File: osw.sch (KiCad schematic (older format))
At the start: 59 parts, among them J1 Conn_01x02, J2 Conn_01x04, J3 Conn_01x02, Q1 2N7002, SW1 SW_Push, SW2 SW_Push, SW4 SW_Push, SW5 SW_Push, U1 DS3231MZ, U10 LTC3440EMS, U11 MCP73831T-2ACI_OT, U12 USBLC6-2SC6, U2 BMA400, U3 BMP280, U4 GC9A01_IPS_display, U5 USB-OTG, U6 CH340E, U7 ttgo-32-micro, U8 Quectel_L96, U9 TPS2115A

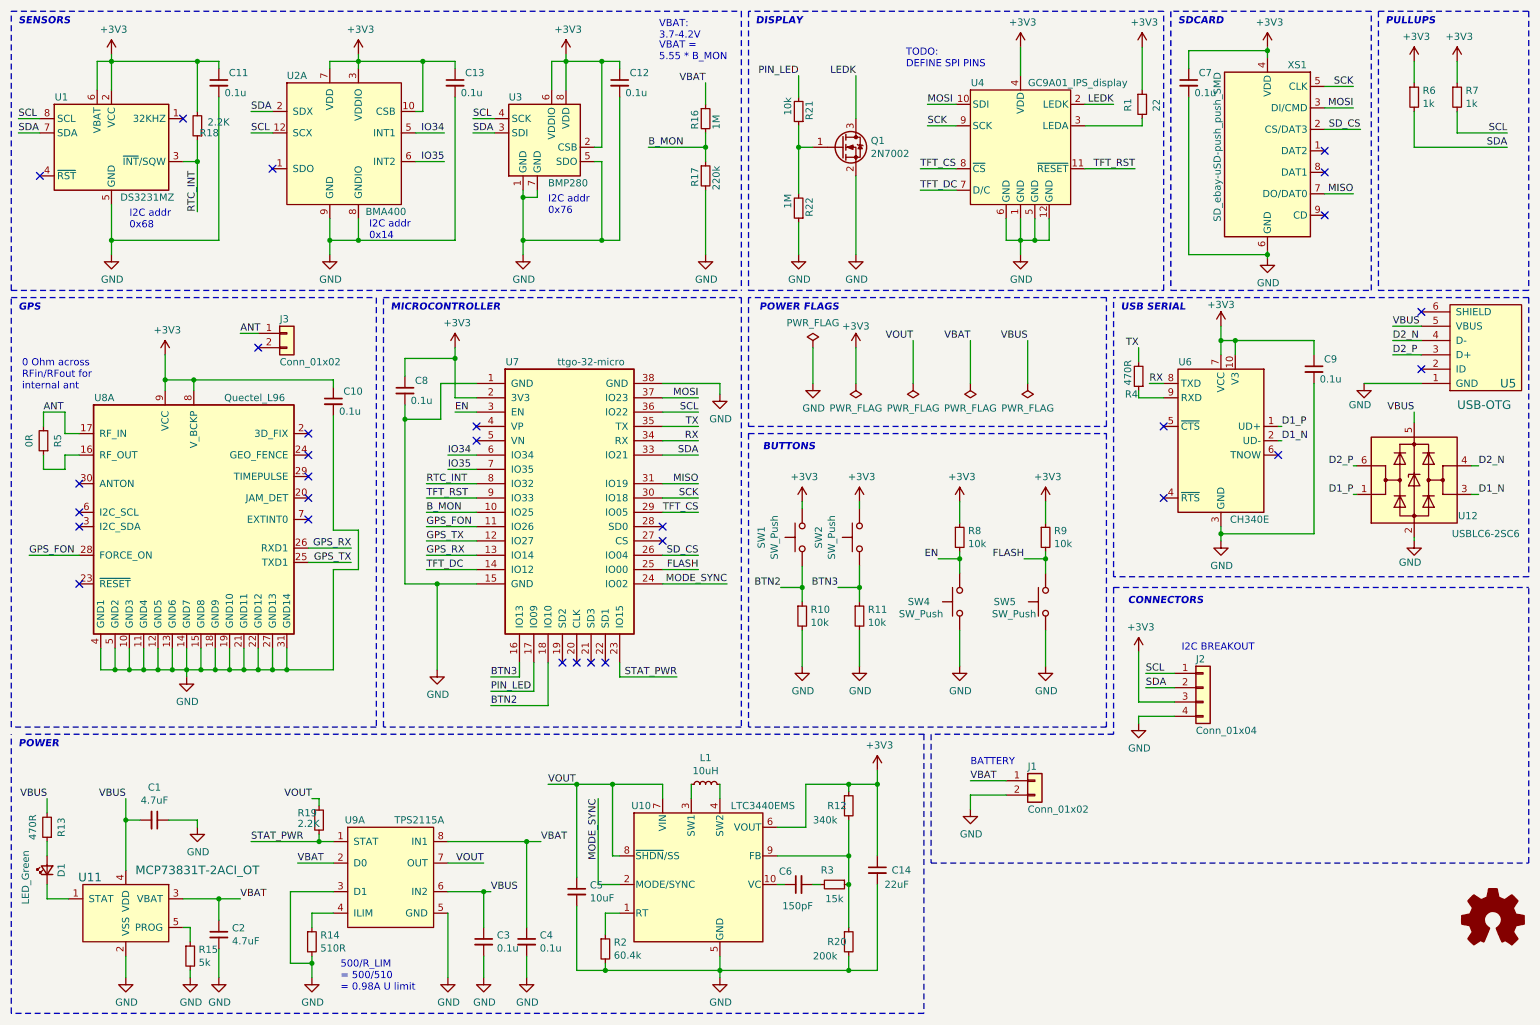
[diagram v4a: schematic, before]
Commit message: add 3V3 to 2V8 Uart shifter
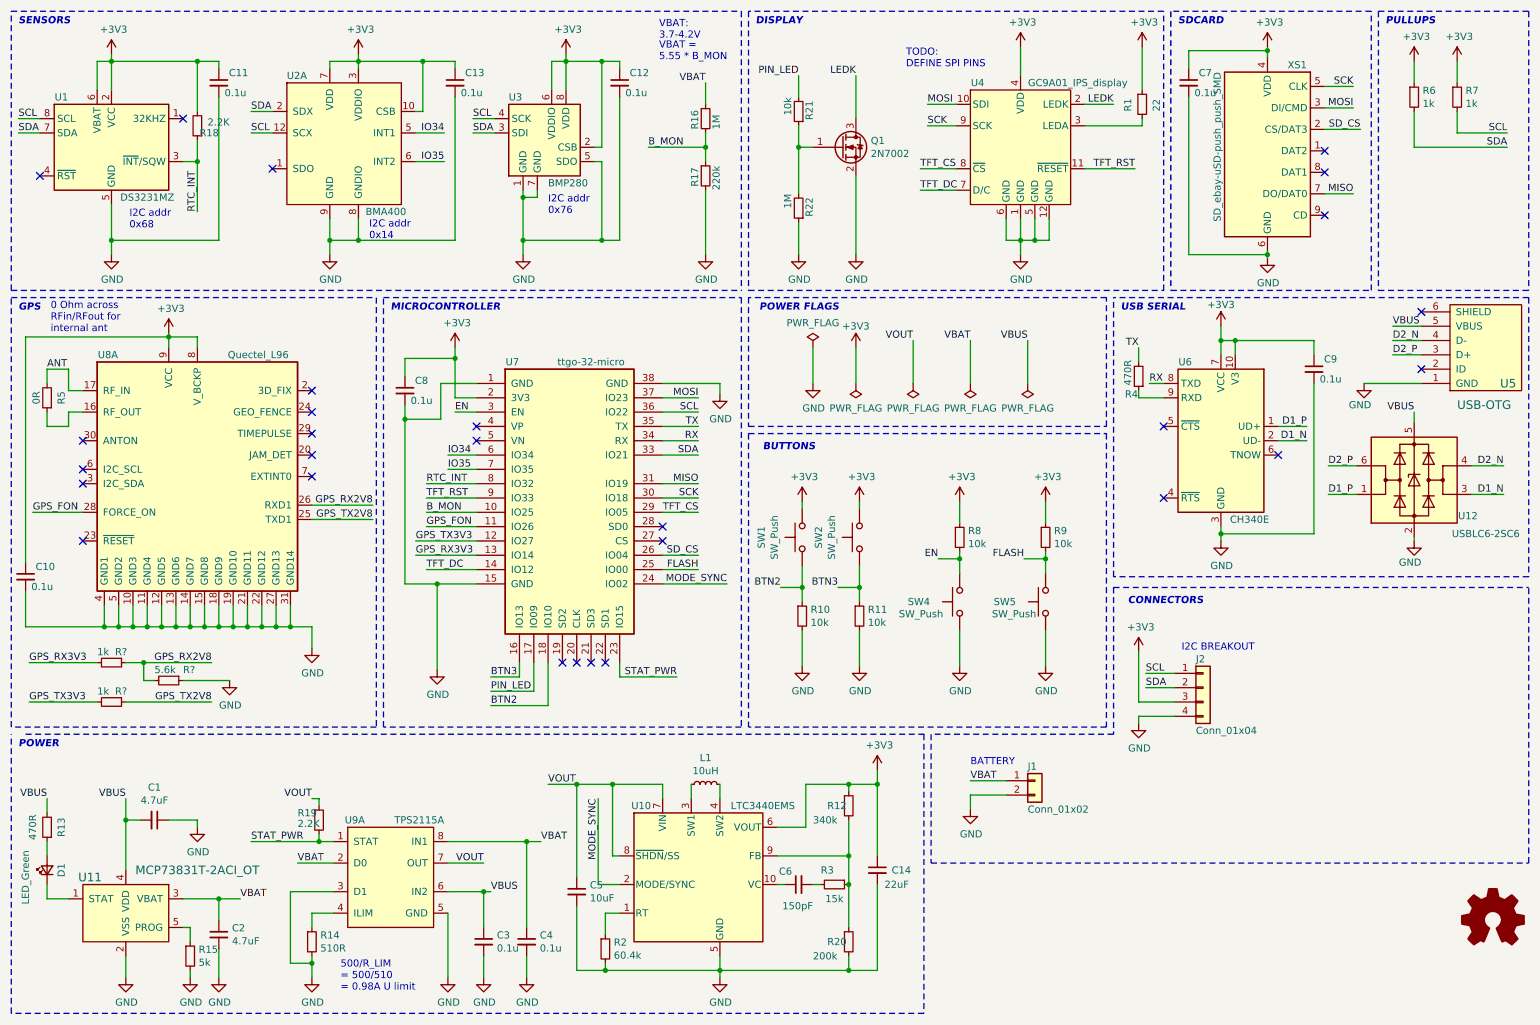
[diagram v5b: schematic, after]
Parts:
- removed J3: Conn_01x02, open-Smartwatch:U.FL_Molex_MCRF_73412-0110_Vertical, symbol Connector_Generic:Conn_01x02
- added R? (x2): 1k, Resistor_SMD:R_0603_1608Metric, symbol Device:R_Small
- added R?: 5.6k, Resistor_SMD:R_0603_1608Metric, symbol Device:R_Small
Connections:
- net GND: now also R?.1
- net GPS_RX renamed GPS_RX2V8
- net GPS_RX2V8: now also R?.1, R?.2; no longer U7.13 (IO14)
- net GPS_TX renamed GPS_TX2V8
- net GPS_TX2V8: now also R?.1; no longer U7.12 (IO27)
- new net GPS_RX3V3: R?.2, U7.13 (IO14)
- new net GPS_TX3V3: R?.2, U7.12 (IO27)
- no-connect marks 29 -> 28
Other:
- moved on the sheet: C10, R5, U8A

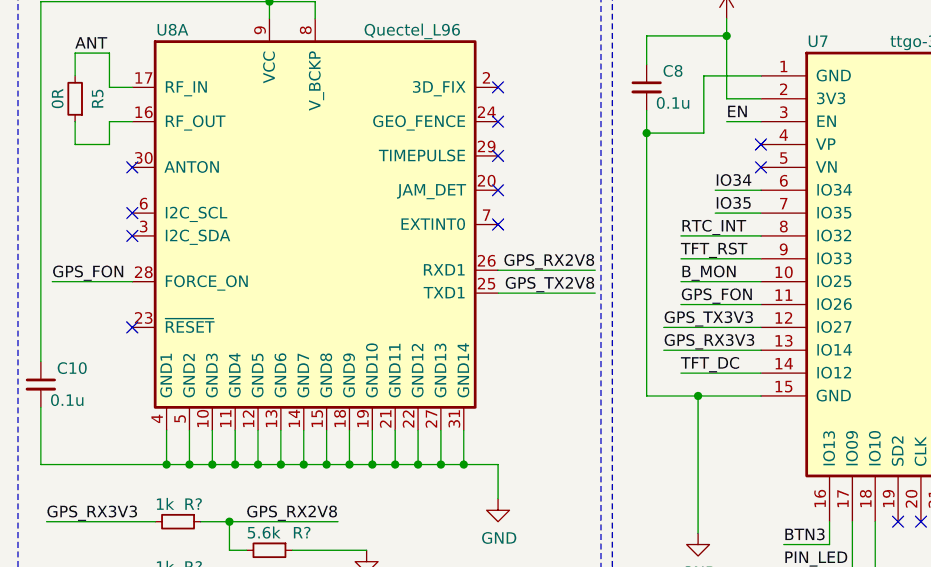
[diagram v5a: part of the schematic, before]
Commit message: disconnect GPS_FON
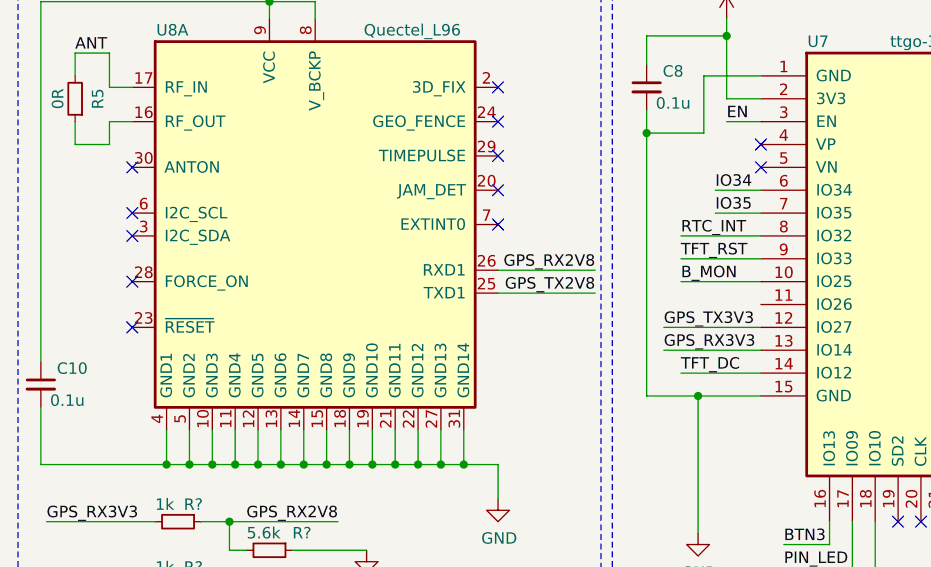
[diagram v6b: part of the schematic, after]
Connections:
- net GPS_FON: no longer names the net of U8.28 (FORCE_ON)
- net GPS_FON: no longer U7.11 (IO26)
- no-connect marks 28 -> 29
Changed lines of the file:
@@
 NoConn ~ 1000 3800
 NoConn ~ 1000 3700
-Text Label 650  4000 0    50   ~ 0
-GPS_FON
-Wire Wire Line
-	650  4000 1000 4000
-Text Label 3400 4100 0    50   ~ 0
-GPS_FON
 Wire Wire Line
 	3400 4000 3750 4000
-Wire Wire Line
-	3400 4100 3750 4100
 Wire Wire Line
 	4150 5250 4150 5050
@@
 Wire Wire Line
 	600  2775 600  4350
-Wire Wire Line
-	2450 4800 2600 4800
-Wire Wire Line
-	2600 4800 2600 4950
 Connection ~ 2450 4800
 Wire Wire Line
@@
 Wire Wire Line
 	1700 5175 2025 5175
+Wire Wire Line
+	2450 4800 2600 4800
+Wire Wire Line
+	2600 4800 2600 4950
+NoConn ~ 1000 4000
 $EndSCHEMATC

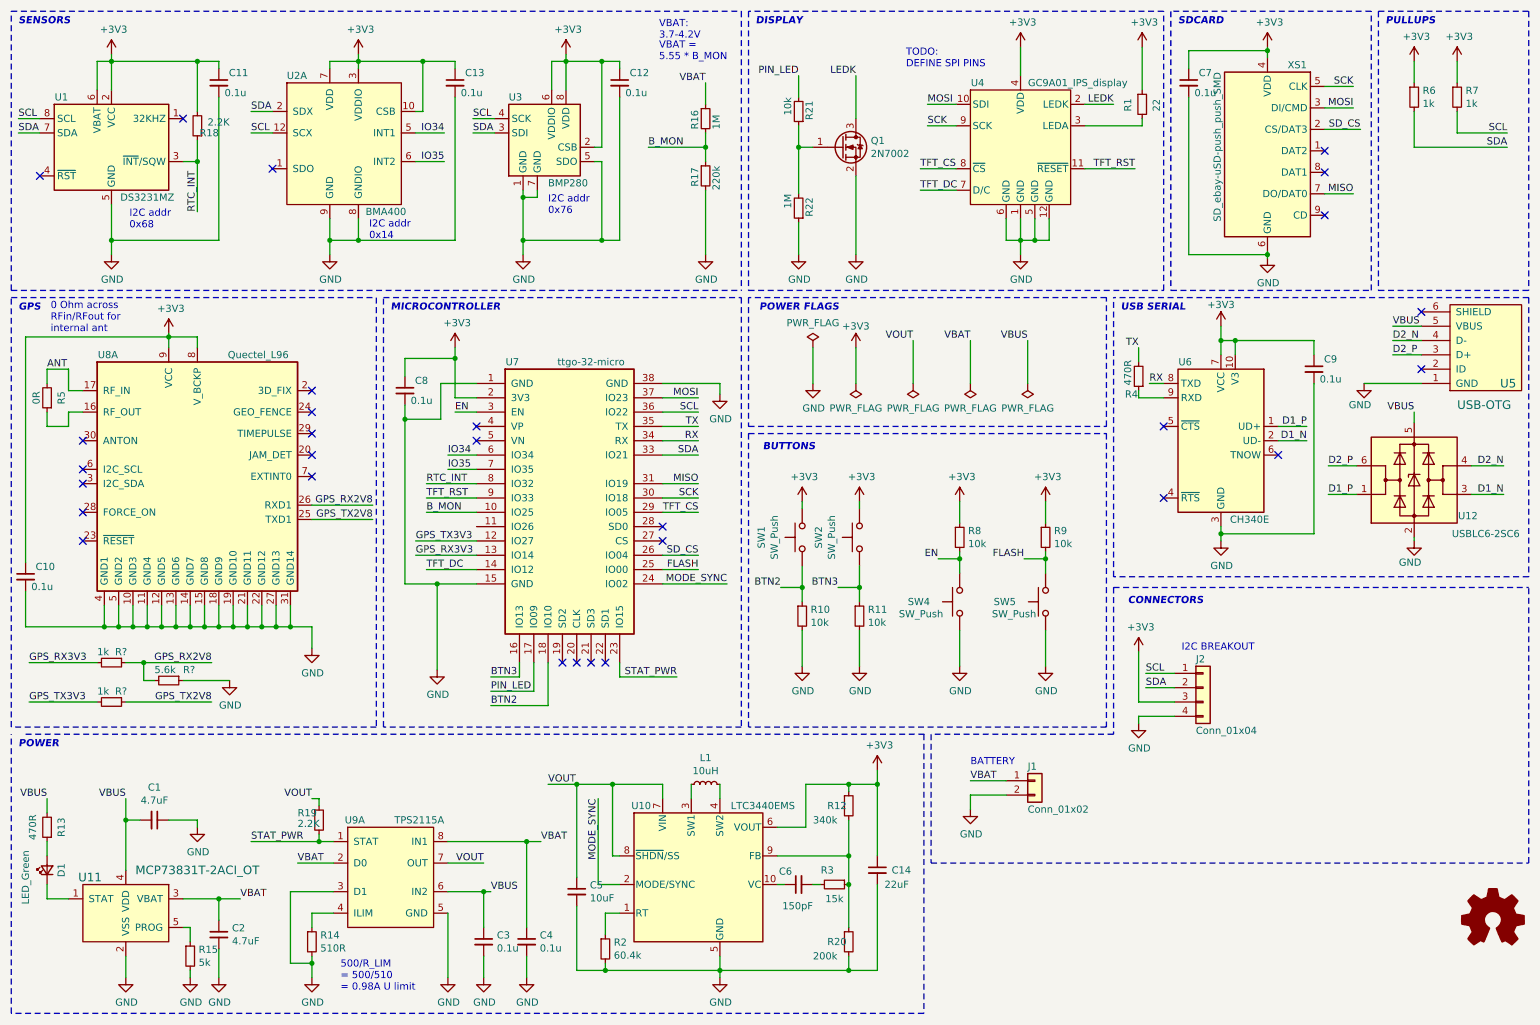
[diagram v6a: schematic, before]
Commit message: replace ltc3440 with 2x XC6209
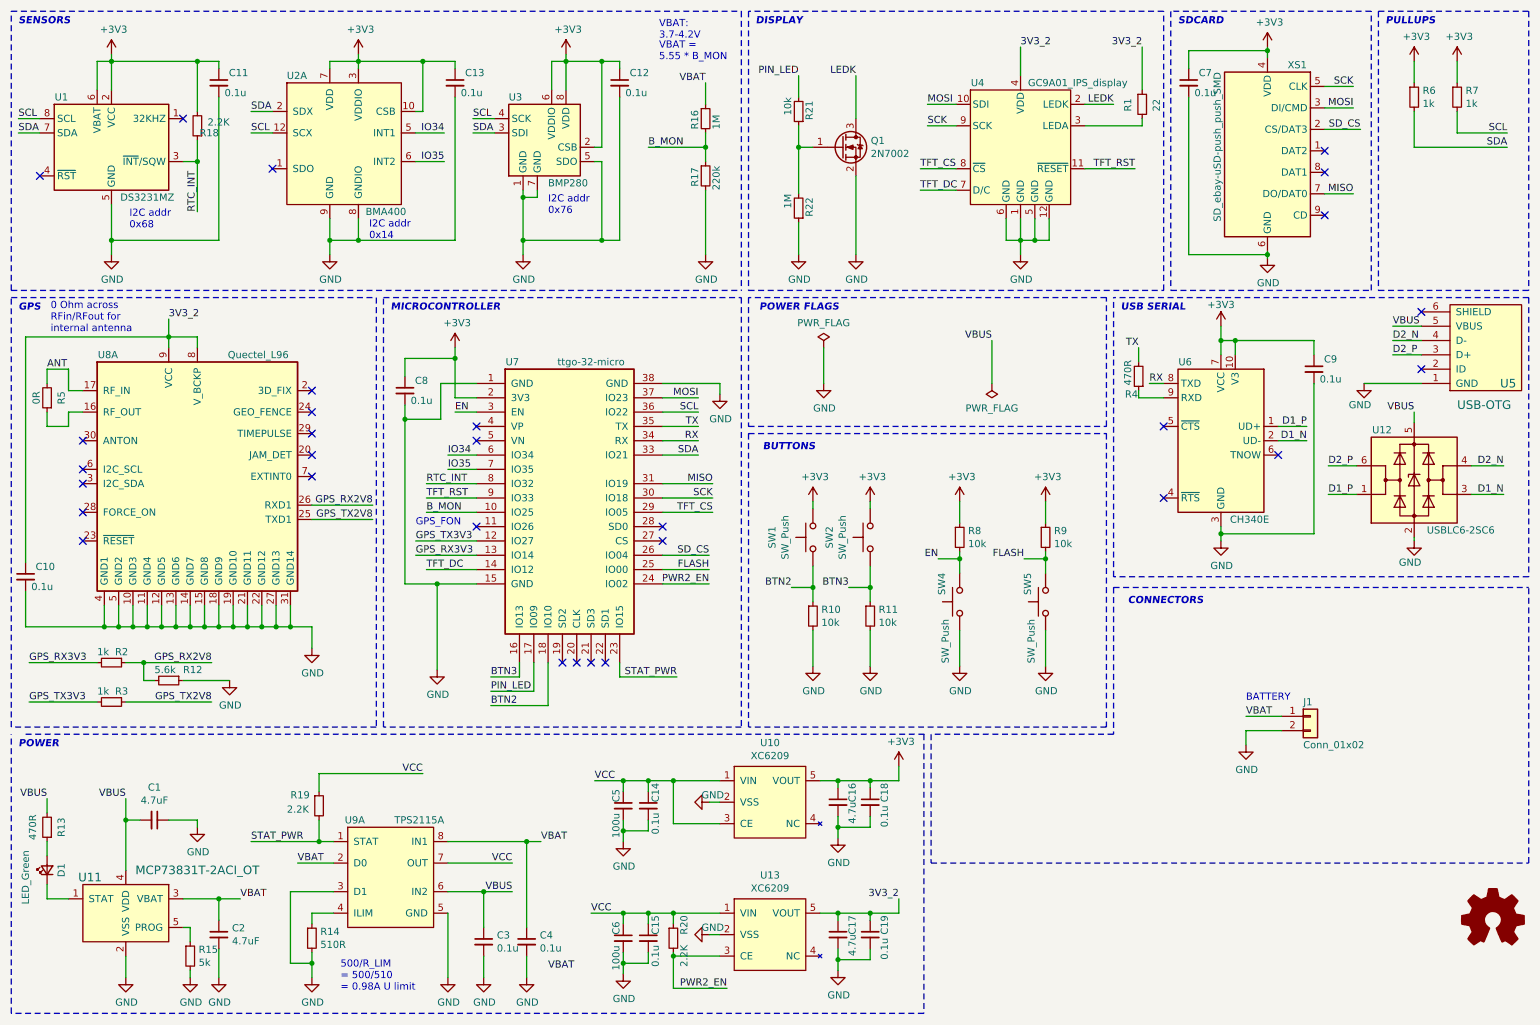
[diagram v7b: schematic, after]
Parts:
- removed J2: Conn_01x04, Connector_PinHeader_1.27mm:PinHeader_1x04_P1.27mm_Vertical, symbol open-Smartwatch:Conn_01x04
- removed L1: 10uH, open-Smartwatch:L_Sumida-CDRH6D38, symbol Device:L_Small
- removed R12: 340k, Resistor_SMD:R_0603_1608Metric, symbol Device:R_Small
- removed R2: 60.4k, Resistor_SMD:R_0603_1608Metric, symbol Device:R_Small
- removed R3: 15k, Resistor_SMD:R_0603_1608Metric, symbol Device:R_Small
- removed U10: LTC3440EMS, Package_SO:MSOP-10_3x3mm_P0.5mm, symbol open-Smartwatch:LTC3440EMS
- added C15, C18, C19: 0.1u, Capacitor_SMD:C_0603_1608Metric, symbol Device:C_Small
- added C16, C17: 4.7u, Capacitor_SMD:C_0603_1608Metric, symbol Device:C_Small
- added U10, U13: XC6209, Package_TO_SOT_SMD:SOT-23-5, symbol open-Smartwatch:XC6209
- C14: value 22uF -> 0.1u; footprint Capacitor_SMD:C_1206_3216Metric -> Capacitor_SMD:C_0603_1608Metric
- C5: value 10uF -> 100u
- C6: value 150pF -> 100u; footprint Capacitor_SMD:C_0603_1608Metric -> Capacitor_SMD:C_1206_3216Metric
- R20: value 200k -> 2.2K
- gave numbers to parts that had none: 3
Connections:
- net VOUT is gone; now on net VCC: C5.1, R19.1, U9.7 (OUT)
- net +3V3: now also C16.1, C18.1, U10.5 (VOUT); no longer C10.1, C14.1, R1.1, U4.4 (VDD), U8.8 (V_BCKP), U8.9 (VCC)
- net GND: now also C6.2, C15.2, C16.2, C17.2, C18.2, C19.2, U10.2 (VSS), U13.2 (VSS); no longer R20.2
- net VCC: now reaches C6.1
- net VCC: now also C14.1, R20.1, C15.1, U10.1 (VIN), U10.3 (CE), U13.1 (VIN)
- net MODE_SYNC renamed PWR2_EN
- net PWR2_EN: now also R20.2, U13.3 (CE)
- new net 3V3_2: C10.1, C17.1, C19.1, R1.1, U13.5 (VOUT), U4.4 (VDD), U8.8 (V_BCKP), U8.9 (VCC)
- no-connect marks 29 -> 30
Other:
- note added: "0 Ohm across\nRFin/RFout for\ninternal antenna"
- note added: "GPS_FON"
- note removed: "0 Ohm across\nRFin/RFout for\ninternal ant"
- note removed: "I2C BREAKOUT"
- note removed: "TODO:\nDEFINE SPI PINS"
- moved on the sheet: J1, R10, R11, R14, R19, SW1, SW2
